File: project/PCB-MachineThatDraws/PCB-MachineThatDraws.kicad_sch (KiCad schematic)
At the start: 29 parts, among them J1 SD_Card_Device, J10 Conn_02x03_Odd_Even, J2 Barrel_Jack_Switch, J3 Switch, J4 Switch, J5 Moteur, J6 Moteur, J7 Screw_Terminal_01x02, J8 Servo-Moteur, J9 Conn_02x03_Odd_Even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

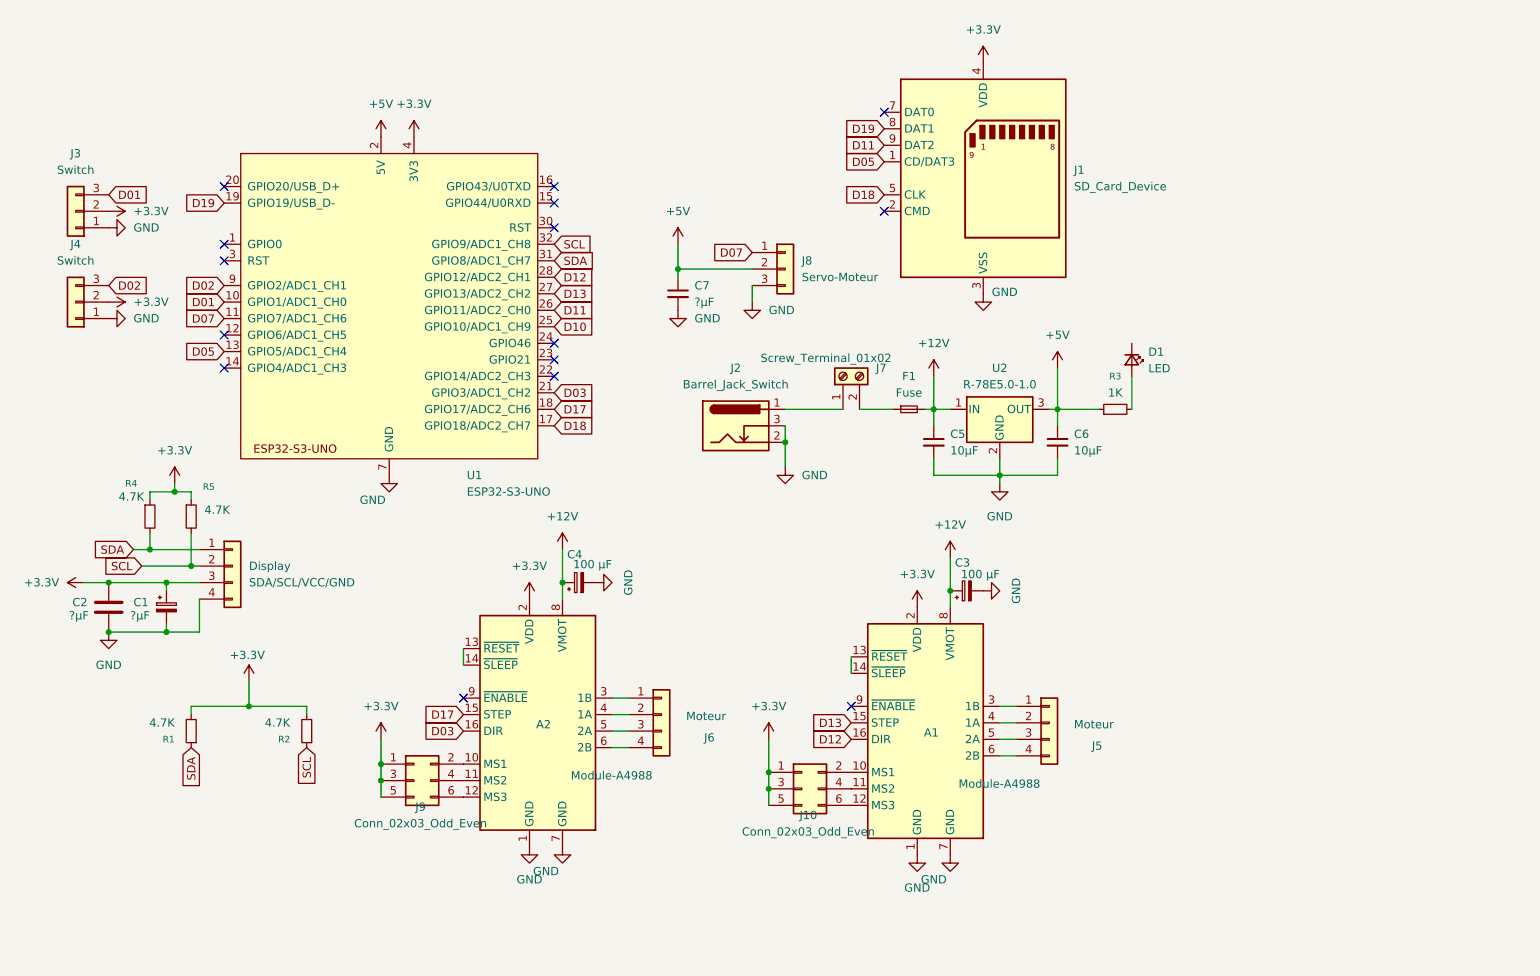
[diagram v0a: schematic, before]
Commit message: update resistor pullup I2C
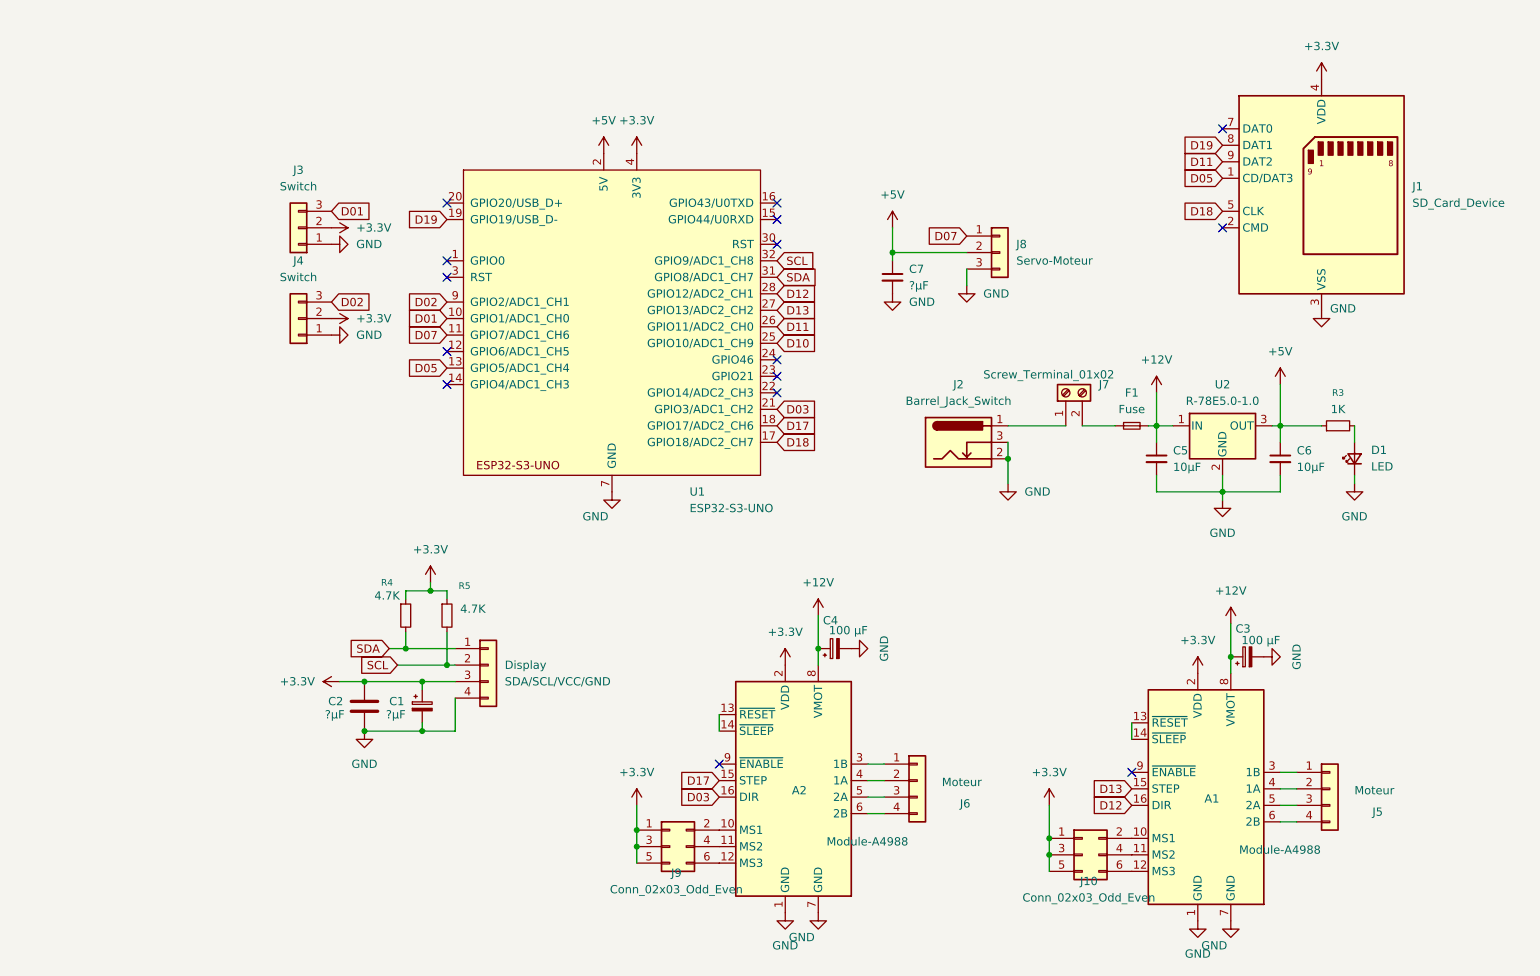
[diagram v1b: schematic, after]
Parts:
- removed R1, R2: 4.7K, symbol makerspace-unilasalle:R
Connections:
- net GND: now also D1.1 (K)
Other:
- moved on the sheet: A1, A2, C1, C2, C3, C4, C5, C6, C7, D1, Display, F1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

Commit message: changement nom / esp / valeur
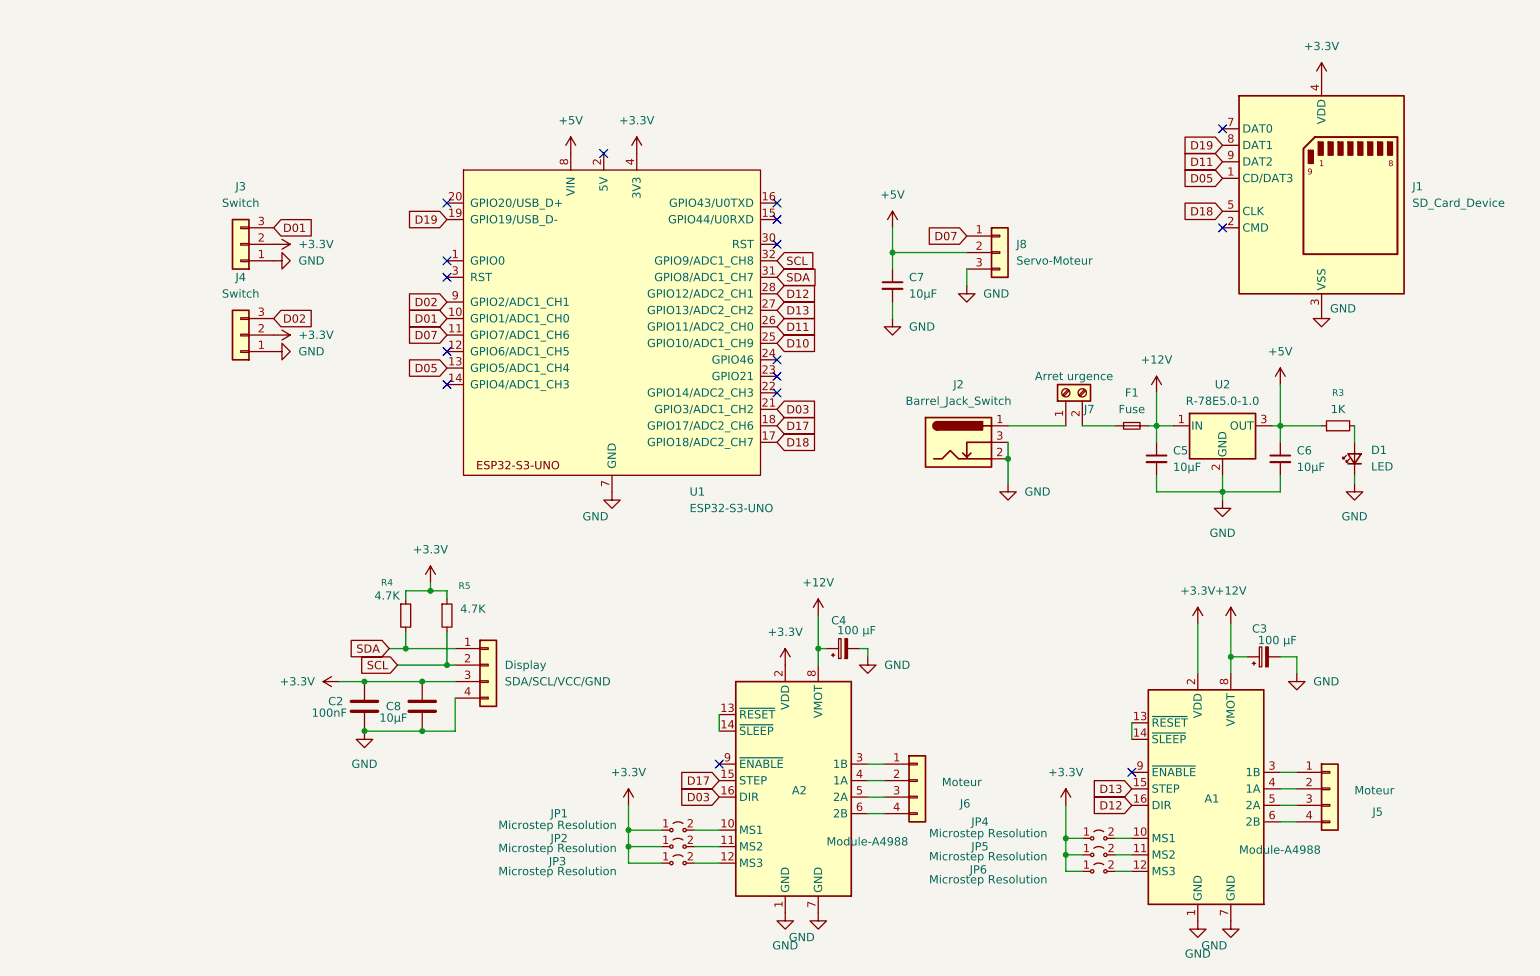
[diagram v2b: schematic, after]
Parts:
- removed C1: ?µF, symbol Device:C_Polarized_Small
- removed J10, J9: Conn_02x03_Odd_Even, symbol Connector_Generic:Conn_02x03_Odd_Even
- added C8: 10µF, makerspace-unilasalle:C_1206, symbol Device:C
- added JP1, JP2, JP3, JP4, JP5, JP6: Microstep Resolution, symbol Jumper:Jumper_2_Small_Open
- C2: value ?µF -> 100nF
- C7: value ?µF -> 10µF
- J7: value Screw_Terminal_01x02 -> Arret urgence
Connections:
- net +3.3V: now also C8.1, JP1.1 (A), JP2.1 (A), JP3.1 (A), JP4.1 (A), JP5.1 (A), JP6.1 (A)
- net +5V: now also U1.8 (VIN); no longer U1.2 (5V)
- net GND: now also C8.2
- net at A1.10 (MS1): now also JP4.2 (B)
- net at A1.11 (MS2): now also JP5.2 (B)
- net at A1.12 (MS3): now also JP6.2 (B)
- net at A2.10 (MS1): now also JP1.2 (B)
- net at A2.11 (MS2): now also JP2.2 (B)
- net at A2.12 (MS3): now also JP3.2 (B)
- no-connect marks 15 -> 16
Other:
- moved on the sheet: C3, C4, C7, J3, J4

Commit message: Kicad
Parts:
- C3, C4: footprint (none) -> Capacitor_SMD:CP_Elec_3x5.3
- C5, C6, C7: footprint (none) -> makerspace-unilasalle:C_1206
- D1: footprint (none) -> LED_THT:LED_D3.0mm_FlatTop
- Display1: renamed from Display; footprint Connector_JST:JST_PH_B3B-PH-K_1x04_P2.00mm_Vertical -> Connector_JST:JST_EH_B4B-EH-A_1x04_P2.50mm_Vertical
- F1: footprint (none) -> Fuse:Fuse_0402_1005Metric
- J2: footprint (none) -> Connector_BarrelJack:BarrelJack_CUI_PJ-036AH-SMT_Horizontal
- J5, J6: footprint Connector_JST:JST_PH_B3B-PH-K_1x04_P2.00mm_Vertical -> Connector_JST:JST_EH_B4B-EH-A_1x04_P2.50mm_Vertical
- J7: footprint (none) -> TerminalBlock_Ningbo-Kagnex:TerminalBlock_Ningbo-Kagnex_HB9500M_1x02_P9.5mm
- J8: footprint (none) -> Connector_JST:JST_EH_B4B-EH-A_1x03_P2.50mm_Vertical
- JP1, JP2, JP3, JP4, JP5, JP6: footprint (none) -> Jumper:Jumper_Harwin_S1621_P10.9mm
- R3, R4, R5: footprint (none) -> makerspace-unilasalle:R_Axial
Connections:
- net +5V: now also R3.2; no longer R3.1
- net at D1.2 (A): now also R3.1; no longer R3.2
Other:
- moved on the sheet: R3
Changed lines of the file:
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@@
 	(wire
 		(pts
+			(xy 129.54 106.68) (xy 129.54 114.3)
+		)
+		(stroke
+			(width 0)
+			(type default)
+		)
+	)
+	(wire
+		(pts
 			(xy 135.89 111.76) (xy 134.62 111.76)
 		)
@@
 			)
 		)
-		(property "Footprint" "Connector_JST:JST_PH_B3B-PH-K_1x04_P2.00mm_Vertical"
+		(property "Footprint" "Connector_JST:JST_EH_B4B-EH-A_1x04_P2.50mm_Vertical"
 			(at 149.86 132.08 0)
 			(effects
@@
 			)
 		)
-		(property "Footprint" ""
+		(property "Footprint" "Jumper:Jumper_Harwin_S1621_P10.9mm"
 			(at 177.8 146.05 0)
 			(effects
@@
 	(symbol
 		(lib_id "power:+3.3V")
-		(at 129.54 114.3 0)
+		(at 129.54 106.68 0)
 		(unit 1)
 		(exclude_from_sim no)
@@
 		(fields_autoplaced yes)
 		(property "Reference" "#PWR017"
-			(at 129.54 118.11 0)
+			(at 129.54 110.49 0)
 			(effects
 				(font
@@
 		)
 		(property "Value" "+3.3V"
-			(at 129.54 109.22 0)
+			(at 129.54 101.6 0)
 			(effects
 				(font
@@
 		)
 		(property "Footprint" ""
-			(at 129.54 114.3 0)
+			(at 129.54 106.68 0)
 			(effects
 				(font
@@
 		)
 		(property "Datasheet" ""
-			(at 129.54 114.3 0)
+			(at 129.54 106.68 0)
 			(effects
 				(font
@@
 		)
 		(property "Description" "Power symbol creates a global label with name \"+3.3V\""
-			(at 129.54 114.3 0)
+			(at 129.54 106.68 0)
 			(effects
 				(font
@@
 			)
 		)
-		(property "Footprint" ""
+		(property "Footprint" "makerspace-unilasalle:C_1206"
 			(at 186.69 82.55 0)
 			(effects
@@
 			)
 		)
-		(property "Footprint" ""
+		(property "Footprint" "TerminalBlock_Ningbo-Kagnex:TerminalBlock_Ningbo-Kagnex_HB9500M_1x02_P9.5mm"
 			(at 172.72 72.39 0)
 			(effects
@@
 			)
 		)
-		(property "Footprint" "Connector_JST:JST_PH_B3B-PH-K_1x04_P2.00mm_Vertical"
+		(property "Footprint" "Connector_JST:JST_EH_B4B-EH-A_1x04_P2.50mm_Vertical"
 			(at 213.36 133.35 0)
 			(effects
@@
 			)
 		)
-		(property "Footprint" ""
+		(property "Footprint" "makerspace-unilasalle:C_1206"
 			(at 205.74 82.55 0)
 			(effects
@@
 			)
 		)
-		(property "Footprint" ""
+		(property "Footprint" "Connector_JST:JST_EH_B4B-EH-A_1x03_P2.50mm_Vertical"
 			(at 162.56 50.8 0)
 			(effects
@@
 			)
 		)
-		(property "Footprint" ""
+		(property "Footprint" "Jumper:Jumper_Harwin_S1621_P10.9mm"
 			(at 113.03 142.24 0)
 			(effects
@@
 			)
 		)
-		(property "Footprint" ""
+		(property "Footprint" "Capacitor_SMD:CP_Elec_3x5.3"
 			(at 203.2 113.03 0)
 			(effects
@@
 	(symbol
 		(lib_id "makerspace-unilasalle:R")
-		(at 214.63 77.47 90)
+		(at 214.63 77.47 270)
 		(unit 1)
 		(exclude_from_sim no)
@@
 			)
 		)
-		(property "Footprint" ""
+		(property "Footprint" "makerspace-unilasalle:R_Axial"
 			(at 214.63 77.47 0)
 			(effects
@@
 			)
 		)
-		(property "Footprint" ""
+		(property "Footprint" "makerspace-unilasalle:C_1206"
 			(at 146.05 55.88 0)
 			(effects
@@
 		(dnp no)
 		(fields_autoplaced yes)
-		(property "Reference" "Display"
+		(property "Reference" "Display1"
 			(at 86.36 114.2999 0)
 			(effects
@@
 			)
 		)
-		(property "Footprint" "Connector_JST:JST_PH_B3B-PH-K_1x04_P2.00mm_Vertical"
+		(property "Footprint" "Connector_JST:JST_EH_B4B-EH-A_1x04_P2.50mm_Vertical"
 			(at 83.82 114.3 0)
 			(effects
@@
 			(project ""
 				(path "/d1309c4d-f5c5-4ae1-9a0a-1ebc6300afdd"
-					(reference "Display")
+					(reference "Display1")
 					(unit 1)
 				)
@@
 			)
 		)
-		(property "Footprint" ""
+		(property "Footprint" "makerspace-unilasalle:R_Axial"
 			(at 77.47 106.68 0)
 			(effects
@@
 			)
 		)
-		(property "Footprint" ""
+		(property "Footprint" "Jumper:Jumper_Harwin_S1621_P10.9mm"
 			(at 177.8 140.97 0)
 			(effects
@@
 			)
 		)
-		(property "Footprint" ""
+		(property "Footprint" "Connector_BarrelJack:BarrelJack_CUI_PJ-036AH-SMT_Horizontal"
 			(at 157.48 81.026 0)
 			(effects
@@
 			)
 		)
-		(property "Footprint" ""
+		(property "Footprint" "Jumper:Jumper_Harwin_S1621_P10.9mm"
 			(at 113.03 144.78 0)
 			(effects
@@
 			)
 		)
-		(property "Footprint" ""
+		(property "Footprint" "makerspace-unilasalle:R_Axial"
 			(at 71.12 106.68 0)
 			(effects
@@
 			)
 		)
-		(property "Footprint" ""
+		(property "Footprint" "Capacitor_SMD:CP_Elec_3x5.3"
 			(at 138.43 111.76 0)
 			(effects
@@
 			)
 		)
-		(property "Footprint" ""
+		(property "Footprint" "Jumper:Jumper_Harwin_S1621_P10.9mm"
 			(at 177.8 143.51 0)
 			(effects
@@
 			)
 		)
-		(property "Footprint" ""
+		(property "Footprint" "LED_THT:LED_D3.0mm_FlatTop"
 			(at 217.17 82.55 90)
 			(effects
@@
 			)
 		)
-		(property "Footprint" ""
+		(property "Footprint" "Jumper:Jumper_Harwin_S1621_P10.9mm"
 			(at 113.03 139.7 0)
 			(effects
@@
 			)
 		)
-		(property "Footprint" ""
+		(property "Footprint" "Fuse:Fuse_0402_1005Metric"
 			(at 182.88 77.47 0)
 			(effects

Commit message: Faire PCB
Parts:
- removed JP1, JP2, JP3, JP4, JP5, JP6: Microstep Resolution, Jumper:Jumper_Harwin_S1621_P10.9mm, symbol Jumper:Jumper_2_Small_Open
- added J10, J9: Conn_02x03_Counter_Clockwise, Connector_PinHeader_2.54mm:PinHeader_2x03_P2.54mm_Vertical, symbol Connector_Generic:Conn_02x03_Counter_Clockwise
- added R6, R7: 10K, makerspace-unilasalle:R_1206, symbol makerspace-unilasalle:R
- C3, C4: footprint Capacitor_SMD:CP_Elec_3x5.3 -> Capacitor_SMD:CP_Elec_6.3x5.4
- D1: footprint LED_THT:LED_D3.0mm_FlatTop -> LED_SMD:LED_1206_3216Metric
- Display1, J5, J6: footprint Connector_JST:JST_EH_B4B-EH-A_1x04_P2.50mm_Vertical -> Connector_PinHeader_2.54mm:PinHeader_1x04_P2.54mm_Vertical
- F1: footprint Fuse:Fuse_0402_1005Metric -> Fuse:Fuseholder_Blade_Mini_Keystone_3568
- J1: footprint (none) -> Connector_Card:SD_Card_Device_16mm_SlotDepth
- J2: footprint Connector_BarrelJack:BarrelJack_CUI_PJ-036AH-SMT_Horizontal -> Connector_BarrelJack:BarrelJack_GCT_DCJ200-10-A_Horizontal
- J3, J4: footprint Connector_JST:JST_PH_B3B-PH-K_1x03_P2.00mm_Vertical -> Connector_PinHeader_2.54mm:PinHeader_1x03_P2.54mm_Vertical
- J7: footprint TerminalBlock_Ningbo-Kagnex:TerminalBlock_Ningbo-Kagnex_HB9500M_1x02_P9.5mm -> TerminalBlock:TerminalBlock_bornier-2_P5.08mm
- J8: footprint Connector_JST:JST_EH_B4B-EH-A_1x03_P2.50mm_Vertical -> Connector_PinHeader_2.54mm:PinHeader_1x03_P2.54mm_Vertical
- R3, R4, R5: footprint makerspace-unilasalle:R_Axial -> makerspace-unilasalle:R_1206
- U1: footprint PCM_Espressif:ESP32-S3-DevKitC -> makerspace-unilasalle:ESP_S3_UNO
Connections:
- net +3.3V: now also J10.4 (Pin_4), J10.5 (Pin_5), J10.6 (Pin_6), J9.4 (Pin_4), J9.5 (Pin_5), J9.6 (Pin_6), R6.1, R7.1
- net D05: now also R7.2
- net D11: now also J1.2 (CMD); no longer J1.9 (DAT2)
- net D19: now also J1.7 (DAT0), U1.12 (GPIO6/ADC1_CH5), R6.2; no longer J1.8 (DAT1), U1.19 (GPIO19/USB_D-)
- net at A1.12 (MS3): now also J10.1 (Pin_1)
- net at A1.10 (MS1): now also J10.3 (Pin_3)
- net at A1.11 (MS2): now also J10.2 (Pin_2)
- net at A2.11 (MS2): now also J9.2 (Pin_2)
- net at A2.12 (MS3): now also J9.1 (Pin_1)
- net at A2.10 (MS1): now also J9.3 (Pin_3)

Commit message: A repenser
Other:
- moved on the sheet: R4
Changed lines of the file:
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@@
 	)
 	(junction
-		(at 168.91 143.51)
+		(at 73.66 102.87)
 		(diameter 0)
 		(color 0 0 0 0)
 	)
 	(junction
-		(at 77.47 114.3)
+		(at 168.91 143.51)
 		(diameter 0)
 		(color 0 0 0 0)
 	)
 	(junction
-		(at 74.93 102.87)
+		(at 77.47 114.3)
 		(diameter 0)
 		(color 0 0 0 0)
@@
 	)
 	(junction
-		(at 71.12 111.76)
+		(at 69.85 111.76)
 		(diameter 0)
 		(color 0 0 0 0)
@@
 	(wire
 		(pts
-			(xy 74.93 101.6) (xy 74.93 102.87)
+			(xy 73.66 101.6) (xy 73.66 102.87)
 		)
 		(stroke
@@
 	(wire
 		(pts
-			(xy 71.12 102.87) (xy 71.12 104.14)
+			(xy 69.85 102.87) (xy 69.85 104.14)
 		)
 		(stroke
@@
 	(wire
 		(pts
-			(xy 69.85 114.3) (xy 77.47 114.3)
-		)
-		(stroke
-			(width 0)
-			(type default)
-		)
-	)
-	(wire
-		(pts
-			(xy 71.12 111.76) (xy 78.74 111.76)
+			(xy 68.58 114.3) (xy 77.47 114.3)
 		)
 		(stroke
@@
 	(wire
 		(pts
-			(xy 77.47 102.87) (xy 74.93 102.87)
-		)
-		(stroke
-			(width 0)
-			(type default)
-		)
-	)
-	(wire
-		(pts
 			(xy 205.74 77.47) (xy 212.09 77.47)
 		)
@@
 	(wire
 		(pts
+			(xy 73.66 102.87) (xy 69.85 102.87)
+		)
+		(stroke
+			(width 0)
+			(type default)
+		)
+	)
+	(wire
+		(pts
 			(xy 217.17 86.36) (xy 217.17 85.09)
 		)
@@
 	(wire
 		(pts
-			(xy 71.12 109.22) (xy 71.12 111.76)
+			(xy 69.85 109.22) (xy 69.85 111.76)
 		)
 		(stroke
@@
 	(wire
 		(pts
+			(xy 69.85 111.76) (xy 78.74 111.76)
+		)
+		(stroke
+			(width 0)
+			(type default)
+		)
+	)
+	(wire
+		(pts
 			(xy 198.12 107.95) (xy 198.12 113.03)
 		)
@@
 	(wire
 		(pts
-			(xy 74.93 102.87) (xy 71.12 102.87)
+			(xy 73.66 102.87) (xy 77.47 102.87)
 		)
 		(stroke
@@
 	(wire
 		(pts
-			(xy 68.58 111.76) (xy 71.12 111.76)
+			(xy 68.58 111.76) (xy 69.85 111.76)
 		)
 		(stroke
@@
 	(global_label "SCL "
 		(shape input)
-		(at 69.85 114.3 180)
+		(at 68.58 114.3 180)
 		(fields_autoplaced yes)
 		(effects
@@
 		)
 		(property "Intersheetrefs" "${INTERSHEET_REFS}"
-			(at 62.3896 114.3 0)
+			(at 61.1196 114.3 0)
 			(effects
 				(font
@@
 	(symbol
 		(lib_id "power:+3.3V")
-		(at 74.93 101.6 0)
+		(at 73.66 101.6 0)
 		(unit 1)
 		(exclude_from_sim no)
@@
 		(fields_autoplaced yes)
 		(property "Reference" "#PWR037"
-			(at 74.93 105.41 0)
+			(at 73.66 105.41 0)
 			(effects
 				(font
@@
 		)
 		(property "Value" "+3.3V"
-			(at 74.93 96.52 0)
+			(at 73.66 96.52 0)
 			(effects
 				(font
@@
 		)
 		(property "Footprint" ""
-			(at 74.93 101.6 0)
+			(at 73.66 101.6 0)
 			(effects
 				(font
@@
 		)
 		(property "Datasheet" ""
-			(at 74.93 101.6 0)
+			(at 73.66 101.6 0)
 			(effects
 				(font
@@
 		)
 		(property "Description" "Power symbol creates a global label with name \"+3.3V\""
-			(at 74.93 101.6 0)
+			(at 73.66 101.6 0)
 			(effects
 				(font
@@
 	(symbol
 		(lib_id "makerspace-unilasalle:R")
-		(at 71.12 106.68 0)
+		(at 69.85 106.68 0)
 		(unit 1)
 		(exclude_from_sim no)
@@
 		(dnp no)
 		(property "Reference" "R4"
-			(at 67.31 101.6 0)
+			(at 66.04 101.6 0)
 			(effects
 				(font
@@
 		)
 		(property "Value" "4.7K"
-			(at 66.294 103.632 0)
+			(at 65.024 103.632 0)
 			(effects
 				(font
@@
 		)
 		(property "Footprint" "makerspace-unilasalle:R_1206"
-			(at 71.12 106.68 0)
+			(at 69.85 106.68 0)
 			(effects
 				(font
@@
 		)
 		(property "Datasheet" "~"
-			(at 71.12 106.68 0)
+			(at 69.85 106.68 0)
 			(effects
 				(font
@@
 		)
 		(property "Description" "Resistor, small symbol"
-			(at 71.12 106.68 0)
+			(at 69.85 106.68 0)
 			(effects
 				(font

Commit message: Peut etre a revoir
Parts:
- J1: footprint Connector_Card:SD_Card_Device_16mm_SlotDepth -> Connector_Card:microSD_HC_Molex_47219-2001
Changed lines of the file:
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@@
 			)
 		)
-		(property "Footprint" "Connector_Card:SD_Card_Device_16mm_SlotDepth"
+		(property "Footprint" "Connector_Card:microSD_HC_Molex_47219-2001"
 			(at 212.09 41.91 0)
 			(effects

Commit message: A verifier
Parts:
- J1: footprint Connector_Card:microSD_HC_Molex_47219-2001 -> makerspace-unilasalle:SD_Hirose_DM1AA_SF_PEJ82
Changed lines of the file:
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@@
 			)
 		)
-		(property "Footprint" "Connector_Card:microSD_HC_Molex_47219-2001"
+		(property "Footprint" "makerspace-unilasalle:SD_Hirose_DM1AA_SF_PEJ82"
 			(at 212.09 41.91 0)
 			(effects

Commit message: fix some wiring problems
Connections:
- net +12V: now also U1.8 (+VIN)
- net +5V: no longer U1.8 (+VIN)
